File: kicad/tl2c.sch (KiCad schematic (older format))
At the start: 33 parts, among them IC101 ATTINY20-X, P101 12VDC, P102 I2C Master, P103 Spare, P104 ISP Header, P105 LED_DRIVER, P106 240VAC, P107 LED_DRIVER, P108 LED_OUT, SW101 TL3315NF160Q

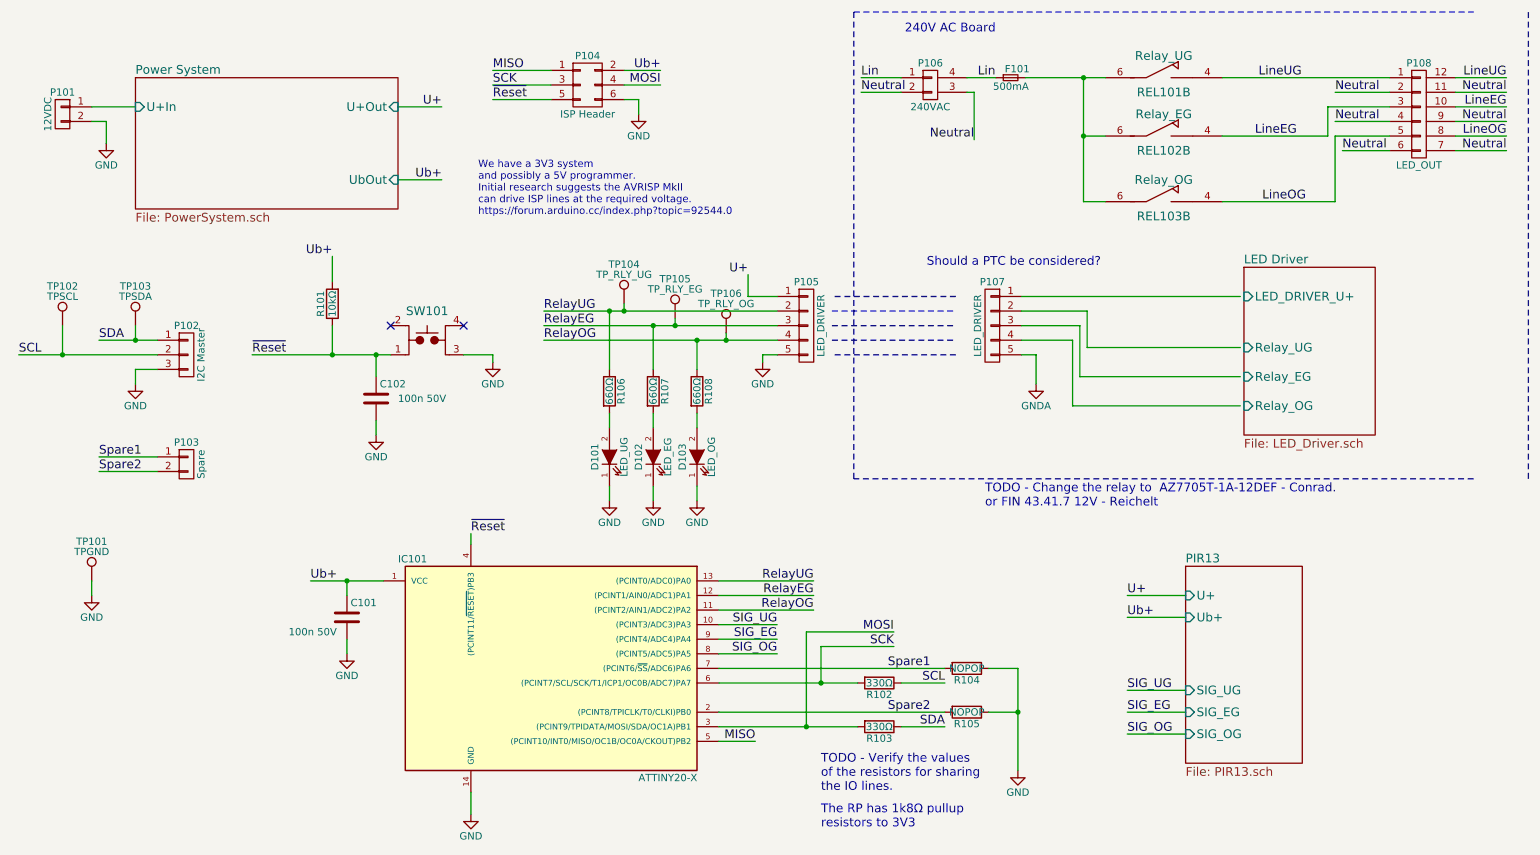
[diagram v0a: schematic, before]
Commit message: Finilised the layout with a larger pin header to expose spare pins to relay driver board
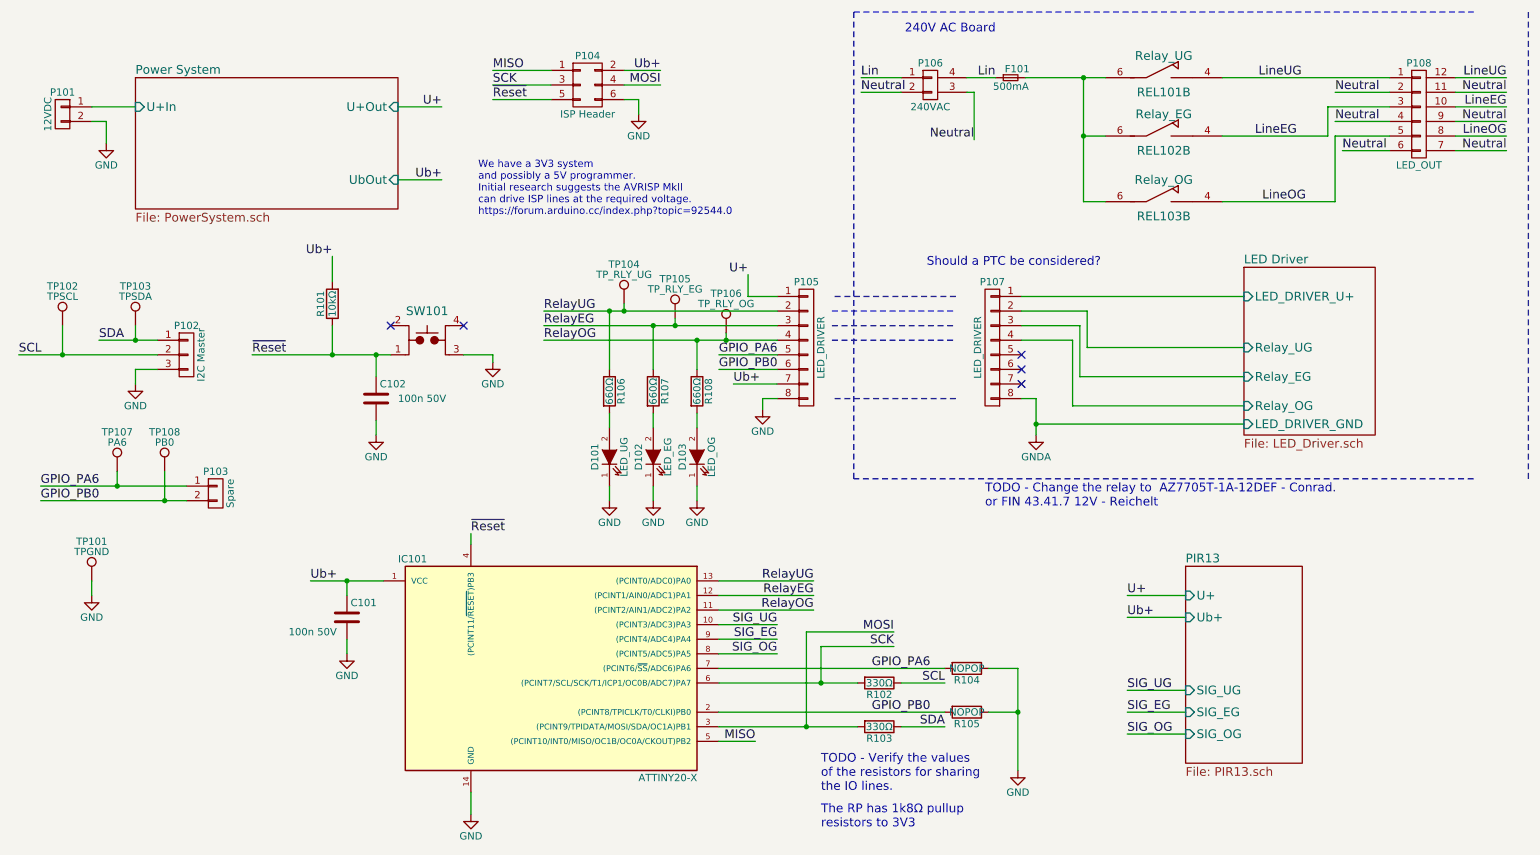
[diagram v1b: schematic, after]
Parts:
- removed P105, P107: LED_DRIVER, Pin_Headers:Pin_Header_Straight_1x05, symbol CONN_01X05
- added P105, P107: LED_DRIVER, Pin_Headers:Pin_Header_Straight_1x08_Pitch2.54mm, symbol CONN_01X08
- added TP107: PA6, Measurement_Points:Measurement_Point_Round-SMD-Pad_Small, symbol TEST_1P
- added TP108: PB0, Measurement_Points:Measurement_Point_Round-SMD-Pad_Small, symbol TEST_1P
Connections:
- net GND: now also P105.8 (P8)
- net GNDA: now also P107.8 (P8)
- net LED Driver/LED_DRIVER_U+: now also P107.1 (P1)
- net LED Driver/Relay_EG: now also P107.3 (P3)
- net LED Driver/Relay_OG: now also P107.4 (P4)
- net LED Driver/Relay_UG: now also P107.2 (P2)
- net RelayEG: now also P105.3 (P3)
- net RelayOG: now also P105.4 (P4)
- net RelayUG: now also P105.2 (P2)
- net U+: now also P105.1 (P1)
- net Ub+: now also P105.7 (P7)
- net Spare1 renamed GPIO_PA6
- net GPIO_PA6: now also P105.5 (P5), TP107.1
- net Spare2 renamed GPIO_PB0
- net GPIO_PB0: now also P105.6 (P6), TP108.1
- no-connect marks 2 -> 5
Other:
- moved on the sheet: P103

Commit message: Fixed some issues with the schematic and layout
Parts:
- removed R102: 330Ω, Resistors_SMD:R_0805, symbol R
- added P109: 5VDC, Pin_Headers:Pin_Header_Straight_1x02, symbol CONN_01X02
- P104: value ISP Header -> TPI Header
- R103: value 330Ω -> 0Ω
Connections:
- net GND: now also P109.2 (P2)
- net SCL: now also IC101.6 ((PCINT7/SCL/SCK/T1/ICP1/OC0B/ADC7)PA7)
- net GPIO_PB0 renamed GPIO_PB2
- net GPIO_PB2: now also IC101.5 ((PCINT10/INT0/MISO/OC1B/OC0A/CKOUT)PB2); no longer IC101.2 ((PCINT8/TPICLK/T0/CLKI)PB0)
- net MISO renamed TPIDATA
- net TPIDATA: now also IC101.3 ((PCINT9/TPIDATA/MOSI/SDA/OC1A)PB1), R103.2; no longer IC101.5 ((PCINT10/INT0/MISO/OC1B/OC0A/CKOUT)PB2)
- removed net MOSI: IC101.3 ((PCINT9/TPIDATA/MOSI/SDA/OC1A)PB1), P104.4 (P4), R103.2
- net SCK renamed TPICLOCK
- net TPICLOCK: no longer IC101.6 ((PCINT7/SCL/SCK/T1/ICP1/OC0B/ADC7)PA7)
- new net Power System/5V: P109.1 (P1)
- new net TPICLK: IC101.2 ((PCINT8/TPICLK/T0/CLKI)PB0)
- no-connect marks 5 -> 6
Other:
- note added: "Ub+ for \nprogramming"
- moved on the sheet: R105
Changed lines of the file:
@@
 Ub+
 $Comp
-L GND #PWR01
+L GND #PWR107
 U 1 1 584C3309
 P 3700 6200
-F 0 "#PWR01" H 3700 5950 50  0001 C CNN
+F 0 "#PWR107" H 3700 5950 50  0001 C CNN
 F 1 "GND" H 3700 6050 50  0000 C CNN
 F 2 "" H 3700 6200 50  0000 C CNN
@@
 $EndComp
 Text Label 3850 1100 0    60   ~ 0
-MISO
+TPIDATA
 Text Label 3850 1200 0    60   ~ 0
-SCK
+TPICLOCK
 Text Label 5000 1100 2    60   ~ 0
 Ub+
-Text Label 5000 1200 2    60   ~ 0
-MOSI
-$Comp
-L GND #PWR02
+$Comp
+L GND #PWR110
 U 1 1 584C39BE
 P 4850 1400
-F 0 "#PWR02" H 4850 1150 50  0001 C CNN
+F 0 "#PWR110" H 4850 1150 50  0001 C CNN
 F 1 "GND" H 4850 1250 50  0000 C CNN
 F 2 "" H 4850 1400 50  0000 C CNN
@@
 $EndComp
 $Comp
-L GND #PWR03
+L GND #PWR105
 U 1 1 584C4458
 P 2850 5100
-F 0 "#PWR03" H 2850 4850 50  0001 C CNN
+F 0 "#PWR105" H 2850 4850 50  0001 C CNN
 F 1 "GND" H 2850 4950 50  0000 C CNN
 F 2 "" H 2850 5100 50  0000 C CNN
@@
 Text Label 2750 2375 2    60   ~ 0
 Ub+
-Text Label 6600 5050 2    60   ~ 0
-SCK
-Text Label 6600 4950 2    60   ~ 0
-MOSI
-Text Label 5650 5700 2    60   ~ 0
-MISO
 $Comp
 L R R103
@@
 P 6500 5600
 F 0 "R103" V 6580 5600 50  0000 C CNN
-F 1 "330Ω" V 6500 5600 50  0000 C CNN
+F 1 "0Ω" V 6500 5600 50  0000 C CNN
 F 2 "Resistors_SMD:R_0805" V 6430 5600 50  0001 C CNN
 F 3 "" H 6500 5600 50  0000 C CNN
@@
 	0    1    1    0
 $EndComp
-$Comp
-L R R102
-U 1 1 584C5F14
-P 6500 5300
-F 0 "R102" V 6580 5300 50  0000 C CNN
-F 1 "330Ω" V 6500 5300 50  0000 C CNN
-F 2 "Resistors_SMD:R_0805" V 6430 5300 50  0001 C CNN
-F 3 "" H 6500 5300 50  0000 C CNN
-	1    6500 5300
-	0    1    1    0
-$EndComp
-Text Label 6950 5300 2    60   ~ 0
-SCL
 Text Label 6950 5600 2    60   ~ 0
 SDA
@@
 L R R105
 U 1 1 584C6E58
-P 7100 5500
-F 0 "R105" V 7180 5500 50  0000 C CNN
-F 1 "NOPOP" V 7100 5500 50  0000 C CNN
-F 2 "Resistors_SMD:R_0805" V 7030 5500 50  0001 C CNN
-F 3 "" H 7100 5500 50  0000 C CNN
-	1    7100 5500
+P 7100 5700
+F 0 "R105" V 7180 5700 50  0000 C CNN
+F 1 "NOPOP" V 7100 5700 50  0000 C CNN
+F 2 "Resistors_SMD:R_0805" V 7030 5700 50  0001 C CNN
+F 3 "" H 7100 5700 50  0000 C CNN
+	1    7100 5700
 	0    1    1    0
 $EndComp
 $Comp
-L GND #PWR04
+L GND #PWR114
 U 1 1 584C7124
 P 7450 5900
-F 0 "#PWR04" H 7450 5650 50  0001 C CNN
+F 0 "#PWR114" H 7450 5650 50  0001 C CNN
 F 1 "GND" H 7450 5750 50  0000 C CNN
 F 2 "" H 7450 5900 50  0000 C CNN
@@
 Text Label 5800 5100 2    60   ~ 0
 SIG_OG
-Text Label 6850 5200 2    60   ~ 0
+Text Label 6650 5200 2    60   ~ 0
 GPIO_PA6
-Text Label 6850 5500 2    60   ~ 0
-GPIO_PB0
+Text Label 5800 5300 2    60   ~ 0
+SCL
 $Comp
 L CONN_01X03 P102
@@
 SCL
 $Comp
-L GND #PWR05
+L GND #PWR104
 U 1 1 584C7C99
 P 1400 3250
-F 0 "#PWR05" H 1400 3000 50  0001 C CNN
+F 0 "#PWR104" H 1400 3000 50  0001 C CNN
 F 1 "GND" H 1400 3100 50  0000 C CNN
 F 2 "" H 1400 3250 50  0000 C CNN
@@
 Neutral
 $Comp
-L GND #PWR06
+L GND #PWR108
 U 1 1 584CB28B
 P 3850 3100
-F 0 "#PWR06" H 3850 2850 50  0001 C CNN
+F 0 "#PWR108" H 3850 2850 50  0001 C CNN
 F 1 "GND" H 3850 2950 50  0000 C CNN
 F 2 "" H 3850 3100 50  0000 C CNN
@@
 F3 "U+Out" I R 3200 1350 60
 F4 "U+In" I L 1400 1350 60
+F5 "5V" I L 1400 1850 60
 $EndSheet
 $Comp
@@
 Ub+
 $Comp
-L GND #PWR07
+L GND #PWR102
 U 1 1 584DF6BA
 P 1200 1600
-F 0 "#PWR07" H 1200 1350 50  0001 C CNN
+F 0 "#PWR102" H 1200 1350 50  0001 C CNN
 F 1 "GND" H 1200 1450 50  0000 C CNN
 F 2 "" H 1200 1600 50  0000 C CNN
@@
 $EndComp
 $Comp
-L GND #PWR08
+L GND #PWR101
 U 1 1 584E33BE
 P 1100 4700
-F 0 "#PWR08" H 1100 4450 50  0001 C CNN
+F 0 "#PWR101" H 1100 4450 50  0001 C CNN
 F 1 "GND" H 1100 4550 50  0000 C CNN
 F 2 "" H 1100 4700 50  0000 C CNN
@@
 $EndSheet
 $Comp
-L GND #PWR09
+L GND #PWR113
 U 1 1 58541B90
 P 5700 3425
-F 0 "#PWR09" H 5700 3175 50  0001 C CNN
+F 0 "#PWR113" H 5700 3175 50  0001 C CNN
 F 1 "GND" H 5700 3275 50  0000 C CNN
 F 2 "" H 5700 3425 50  0000 C CNN
@@
 $EndComp
 $Comp
-L GND #PWR010
+L GND #PWR109
 U 1 1 5856AF1B
 P 4650 4050
-F 0 "#PWR010" H 4650 3800 50  0001 C CNN
+F 0 "#PWR109" H 4650 3800 50  0001 C CNN
 F 1 "GND" H 4650 3900 50  0000 C CNN
 F 2 "" H 4650 4050 50  0000 C CNN
@@
 $EndComp
 $Comp
-L GND #PWR011
+L GND #PWR111
 U 1 1 5856B284
 P 4950 4050
-F 0 "#PWR011" H 4950 3800 50  0001 C CNN
+F 0 "#PWR111" H 4950 3800 50  0001 C CNN
 F 1 "GND" H 4950 3900 50  0000 C CNN
 F 2 "" H 4950 4050 50  0000 C CNN
@@
 $EndComp
 $Comp
-L GND #PWR012
+L GND #PWR112
 U 1 1 5856B510
 P 5250 4050
-F 0 "#PWR012" H 5250 3800 50  0001 C CNN
+F 0 "#PWR112" H 5250 3800 50  0001 C CNN
 F 1 "GND" H 5250 3900 50  0000 C CNN
 F 2 "" H 5250 4050 50  0000 C CNN
@@
 $EndComp
 $Comp
-L GNDA #PWR013
+L GNDA #PWR115
 U 1 1 5856E00B
 P 7575 3600
-F 0 "#PWR013" H 7575 3350 50  0001 C CNN
+F 0 "#PWR115" H 7575 3350 50  0001 C CNN
 F 1 "GNDA" H 7575 3450 50  0000 C CNN
 F 2 "" H 7575 3600 50  0000 C CNN
@@
 P 4500 1200
 F 0 "P104" H 4500 1400 50  0000 C CNN
-F 1 "ISP Header" H 4500 1000 50  0000 C CNN
+F 1 "TPI Header" H 4500 1000 50  0000 C CNN
 F 2 "Pin_Headers:Pin_Header_Straight_2x03" H 4500 0   50  0001 C CNN
 F 3 "" H 4500 0   50  0000 C CNN
@@
 $EndComp
 $Comp
-L GND #PWR014
+L GND #PWR106
 U 1 1 5867873E
 P 3050 3600
-F 0 "#PWR014" H 3050 3350 50  0001 C CNN
+F 0 "#PWR106" H 3050 3350 50  0001 C CNN
 F 1 "GND" H 3050 3450 50  0000 C CNN
 F 2 "" H 3050 3600 50  0000 C CNN
@@
 GPIO_PA6
 Text Label 5400 3150 0    60   ~ 0
-GPIO_PB0
+GPIO_PB2
 Text Label 750  3950 0    60   ~ 0
 GPIO_PA6
 Text Label 750  4050 0    60   ~ 0
-GPIO_PB0
+GPIO_PB2
 $Comp
 L CONN_01X08 P107
@@
 	1    0    0    -1
 $EndComp
+NoConn ~ 4750 1200
+Text Label 6600 4950 2    60   ~ 0
+TPIDATA
+Text Label 5800 5500 2    60   ~ 0
+TPICLK
+Text Label 5800 5700 2    60   ~ 0
+GPIO_PB2
 Wire Wire Line
 	2600 4600 3100 4600
@@
 	4750 1100 5000 1100
 Wire Wire Line
-	4750 1200 5000 1200
-Wire Wire Line
 	4750 1300 4850 1300
 Wire Wire Line
@@
 	5400 5600 6350 5600
 Wire Wire Line
-	5400 5700 5650 5700
-Wire Wire Line
-	5400 5300 6350 5300
-Wire Wire Line
-	6650 5300 6950 5300
+	5400 5300 5800 5300
 Wire Wire Line
 	6650 5600 6950 5600
@@
 	5400 5200 6950 5200
 Wire Wire Line
-	5400 5500 6950 5500
-Wire Wire Line
 	7250 5200 7450 5200
 Wire Wire Line
 	7450 5200 7450 5900
-Wire Wire Line
-	7250 5500 7450 5500
-Connection ~ 7450 5500
 Wire Wire Line
 	1150 2950 1550 2950
@@
 	10000 1250 9625 1250
 Wire Wire Line
-	1750 3950 750  3950
-Wire Wire Line
-	1750 4050 750  4050
+	750  3950 1750 3950
+Wire Wire Line
+	750  4050 1750 4050
 Wire Wire Line
 	3650 3050 3850 3050
@@
 	5600 2650 5600 2500
 Wire Notes Line
-	6325 700  10575 700
+	6325 700  10951 696
 Wire Notes Line
 	10950 700  10950 3900
 Wire Notes Line
-	10575 3900 6325 3900
+	10950 3900 6325 3900
 Wire Notes Line
 	6325 3900 6325 700
@@
 	3050 3500 3050 3600
 Wire Wire Line
-	6100 5300 6100 5050
-Wire Wire Line
-	6100 5050 6600 5050
-Connection ~ 6100 5300
-Wire Wire Line
 	6000 5600 6000 4950
 Wire Wire Line
@@
 	9000 3525 7575 3525
 Connection ~ 7575 3525
+Wire Wire Line
+	5400 5700 6950 5700
+Wire Wire Line
+	7250 5700 7450 5700
+Connection ~ 7450 5700
+Wire Wire Line
+	5400 5500 5800 5500
+$Comp
+L CONN_01X02 P109
+U 1 1 589A46DF
+P 900 1900
+F 0 "P109" H 900 2050 50  0000 C CNN
+F 1 "5VDC" V 1000 1900 50  0000 C CNN
+F 2 "Pin_Headers:Pin_Header_Straight_1x02" H 900 1900 50  0001 C CNN
+F 3 "" H 900 1900 50  0000 C CNN
+F 4 "Value" H 900 1900 60  0001 C CNN "MFP"
+F 5 "Value" H 900 1900 60  0001 C CNN "Conrad-PN"
+F 6 "Value" H 900 1900 60  0001 C CNN "Digikey-PN"
+	1    900  1900
+	-1   0    0    -1
+$EndComp
+Wire Wire Line
+	1100 1850 1400 1850
+$Comp
+L GND #PWR103
+U 1 1 589A5184
+P 1250 2100
+F 0 "#PWR103" H 1250 1850 50  0001 C CNN
+F 1 "GND" H 1250 1950 50  0000 C CNN
+F 2 "" H 1250 2100 50  0000 C CNN
+F 3 "" H 1250 2100 50  0000 C CNN
+	1    1250 2100
+	1    0    0    -1
+$EndComp
+Wire Wire Line
+	1100 1950 1250 1950
+Wire Wire Line
+	1250 1950 1250 2100
+Text Notes 550  2200 0    60   ~ 0
+Ub+ for \nprogramming
 $EndSCHEMATC
